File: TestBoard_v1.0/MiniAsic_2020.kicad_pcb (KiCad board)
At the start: 2 copper layers, 1 part

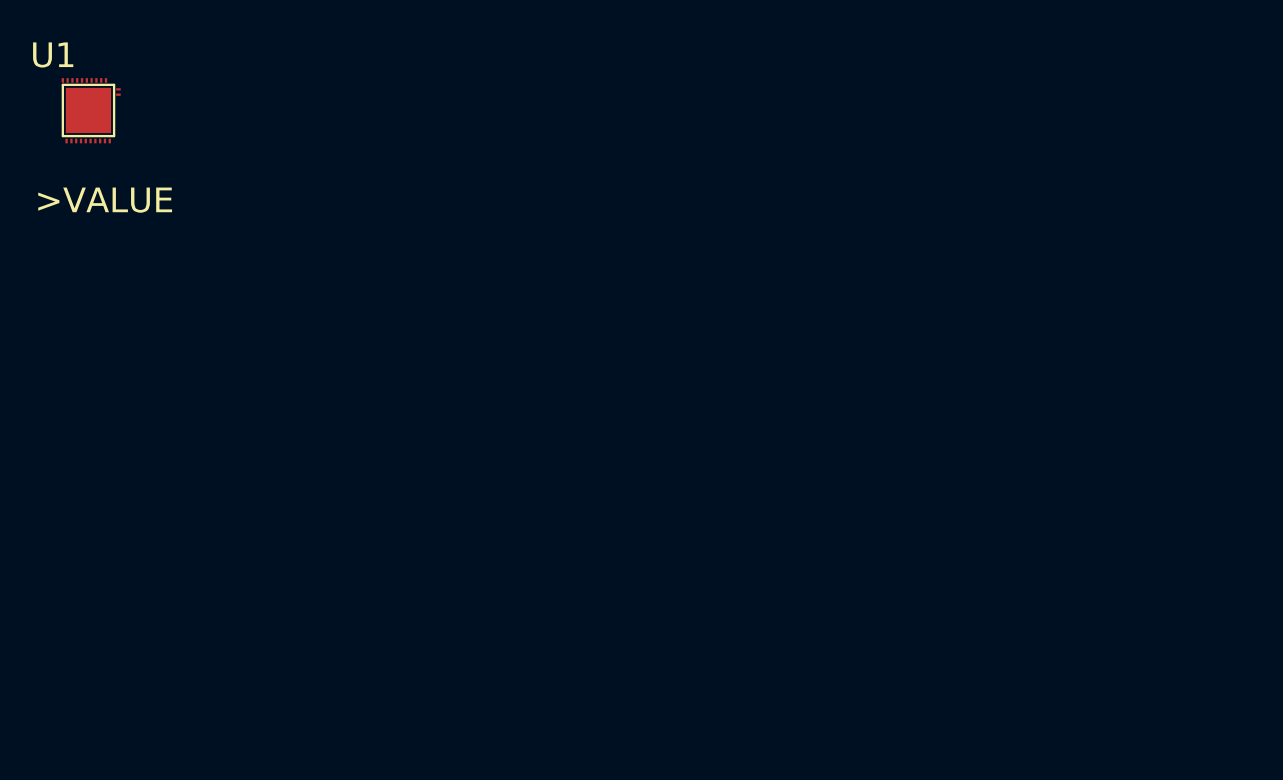
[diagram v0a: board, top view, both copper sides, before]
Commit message: Schematic update and initial placement
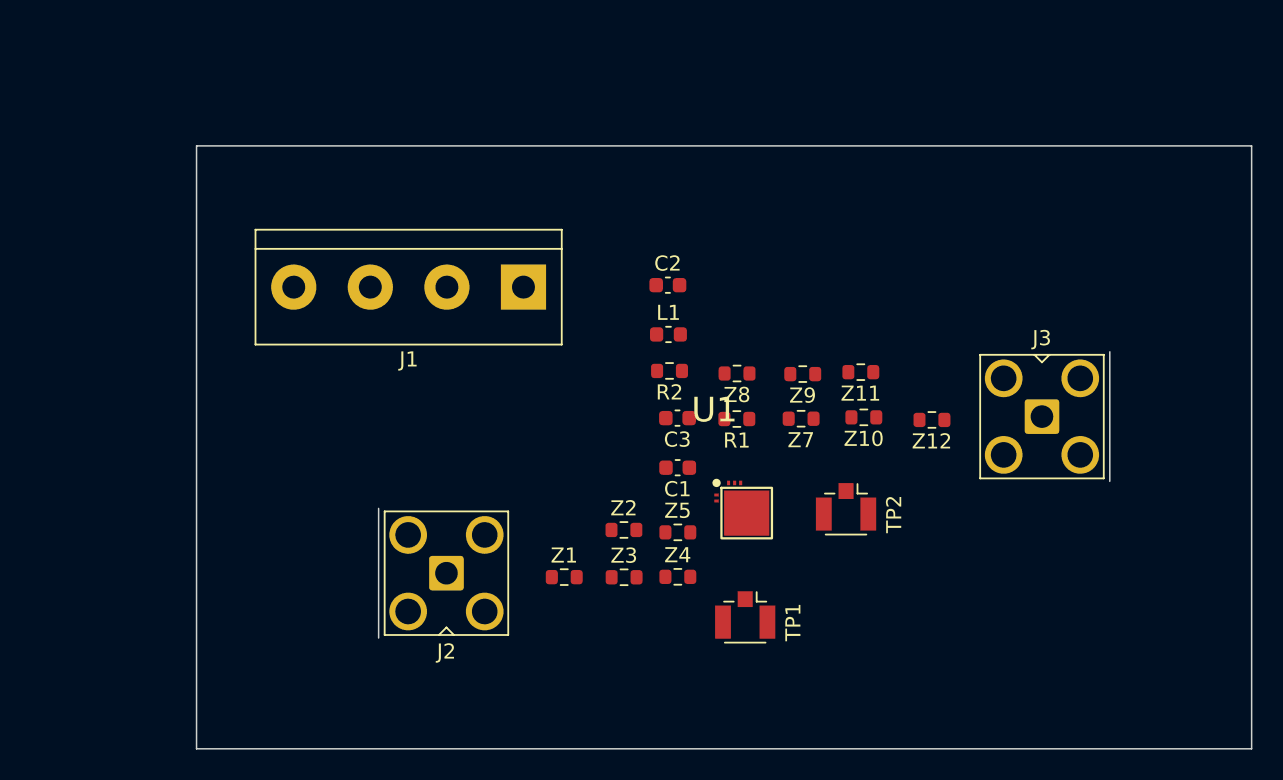
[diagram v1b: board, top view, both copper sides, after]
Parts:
- added C1: C, Capacitor_SMD:C_0603_1608Metric, F.Cu at (176.8, 121.6)
- added C2: C, Capacitor_SMD:C_0603_1608Metric, F.Cu at (176.2, 109.5)
- added C3: C, Capacitor_SMD:C_0603_1608Metric, F.Cu at (176.8, 118.3)
- added J1: Screw_Terminal_01x04, TerminalBlock:TerminalBlock_bornier-4_P5.08mm, F.Cu at (166.6, 109.6)
- added J2: Conn_Coaxial, Connector_Coaxial:SMA_Amphenol_901-143_Horizontal, F.Cu at (161.5, 128.6)
- added J3: Conn_Coaxial, Connector_Coaxial:SMA_Amphenol_901-143_Horizontal, F.Cu at (201.0, 118.2)
- added L1: L, Inductor_SMD:L_0603_1608Metric, F.Cu at (176.2, 112.8)
- added R1: R, Resistor_SMD:R_0603_1608Metric, F.Cu at (180.7, 118.4)
- added R2: R, Resistor_SMD:R_0603_1608Metric, F.Cu at (176.3, 115.2)
- added TP1: ~, Connector_Coaxial:U.FL_Hirose_U.FL-R-SMT-1_Vertical, F.Cu at (181.3, 131.4)
- added TP2: ~, Connector_Coaxial:U.FL_Hirose_U.FL-R-SMT-1_Vertical, F.Cu at (188.0, 124.2)
- added Z1: Z, Resistor_SMD:R_0603_1608Metric, F.Cu at (169.3, 128.8)
- added Z10: Z, Resistor_SMD:R_0603_1608Metric, F.Cu at (189.2, 118.2)
- added Z11: Z, Resistor_SMD:R_0603_1608Metric, F.Cu at (188.9, 115.2)
- added Z12: Z, Resistor_SMD:R_0603_1608Metric, F.Cu at (193.7, 118.4)
- added Z2: Z, Resistor_SMD:R_0603_1608Metric, F.Cu at (173.2, 125.7)
- added Z3: Z, Resistor_SMD:R_0603_1608Metric, F.Cu at (173.2, 128.9)
- added Z4: Z, Resistor_SMD:R_0603_1608Metric, F.Cu at (176.8, 128.8)
- added Z5: Z, Resistor_SMD:R_0603_1608Metric, F.Cu at (176.8, 125.9)
- added Z7: Z, Resistor_SMD:R_0603_1608Metric, F.Cu at (185.0, 118.3)
- added Z8: Z, Resistor_SMD:R_0603_1608Metric, F.Cu at (180.7, 115.3)
- added Z9: Z, Resistor_SMD:R_0603_1608Metric, F.Cu at (185.1, 115.4)
- moved U1 49.8 mm to (179.9, 123.1)
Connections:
- U1 pad 1: unconnected-(U1-IN-Pad1) -> +1V8
- U1 pad 2: GNDREF -> /IN
- U1 pad 3: +1V8 -> /VG_GATED
- U1 pad 4: /VG -> /OUT
- U1 pad 5: GNDREF -> /OUT
- U1 pad 6: /VOUT -> Net-(#PWR025-GND)
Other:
- board outline added: 70 x 40 mm

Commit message: Initial routing
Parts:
- moved TP2 18.0 mm to (205.0, 130.0), turned to 0 degrees
- moved J3 14.1 mm to (215.0, 120.0)
- moved J1 12.5 mm to (155.0, 105.0), turned to -90 degrees
- moved Z11 12.0 mm to (200.0, 120.0)
- moved Z12 11.8 mm to (205.0, 115.0)
- moved Z10 11.3 mm to (200.0, 115.0)
- moved Z9 10.9 mm to (195.0, 120.0)
- moved Z7 10.6 mm to (195.0, 115.0)
- moved Z8 10.4 mm to (190.0, 120.0)
- moved C2 10.2 mm to (180.0, 100.0)
- moved L1 8.64 mm to (180.0, 105.0)
- moved U1 7.02 mm to (186.8, 124.3)
- moved J2 6.61 mm to (155.0, 130.0)
- moved R2 6.38 mm to (180.0, 110.0)
- moved C3 4.60 mm to (180.0, 115.0)
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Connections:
- TP1 pad 1: Net-(#PWR030-GND) -> /TP1
- TP1 pad 2: /TP1 -> Net-(TP1-GND)
- TP2 pad 1: Net-(#PWR031-GND) -> /TP2
- TP2 pad 2: /TP2 -> Net-(TP2-GND)
- Z10 pad 2: Net-(Z10-Pad2) -> /TP2
- Z11 pad 1: /TP2 -> Net-(T2-Pad1)
- Z11 pad 2: Net-(Z10-Pad2) -> /TP2
- Z12 pad 2: /TP2 -> Net-(T2-Pad1)
- Z9 pad 1: Net-(Z10-Pad2) -> /TP2
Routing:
- net +1V8: track 0.00 -> 35.2 mm
- net +3.3V: track 0.00 -> 29.2 mm
- net /OUT: track 0.00 -> 28.8 mm
- net /VG: track 0.00 -> 24.3 mm
- net /TP2: track 0.00 -> 21.7 mm
- net /TP1: track 0.00 -> 17.4 mm
- net /VG_GATED: track 0.00 -> 17.2 mm
- net Net-(Z1-Pad2): track 0.00 -> 10.4 mm
- net Net-(T2-Pad1): track 0.00 -> 6.39 mm
- net /IN: track 0.00 -> 5.48 mm
- net Net-(Z8-Pad1): track 0.00 -> 3.35 mm
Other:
- board size 70 x 40 mm -> 80 x 45 mm

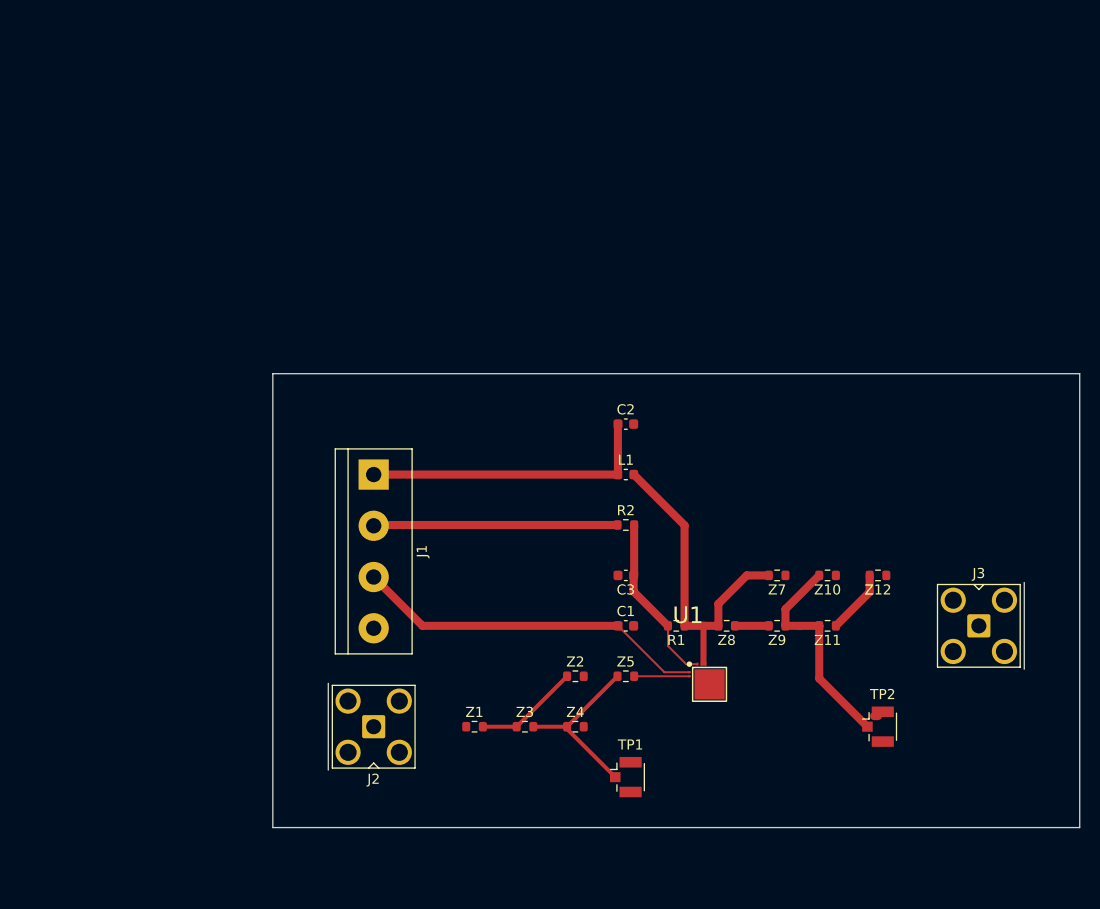
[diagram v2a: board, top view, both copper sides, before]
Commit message: New placement focused on the transmission lines
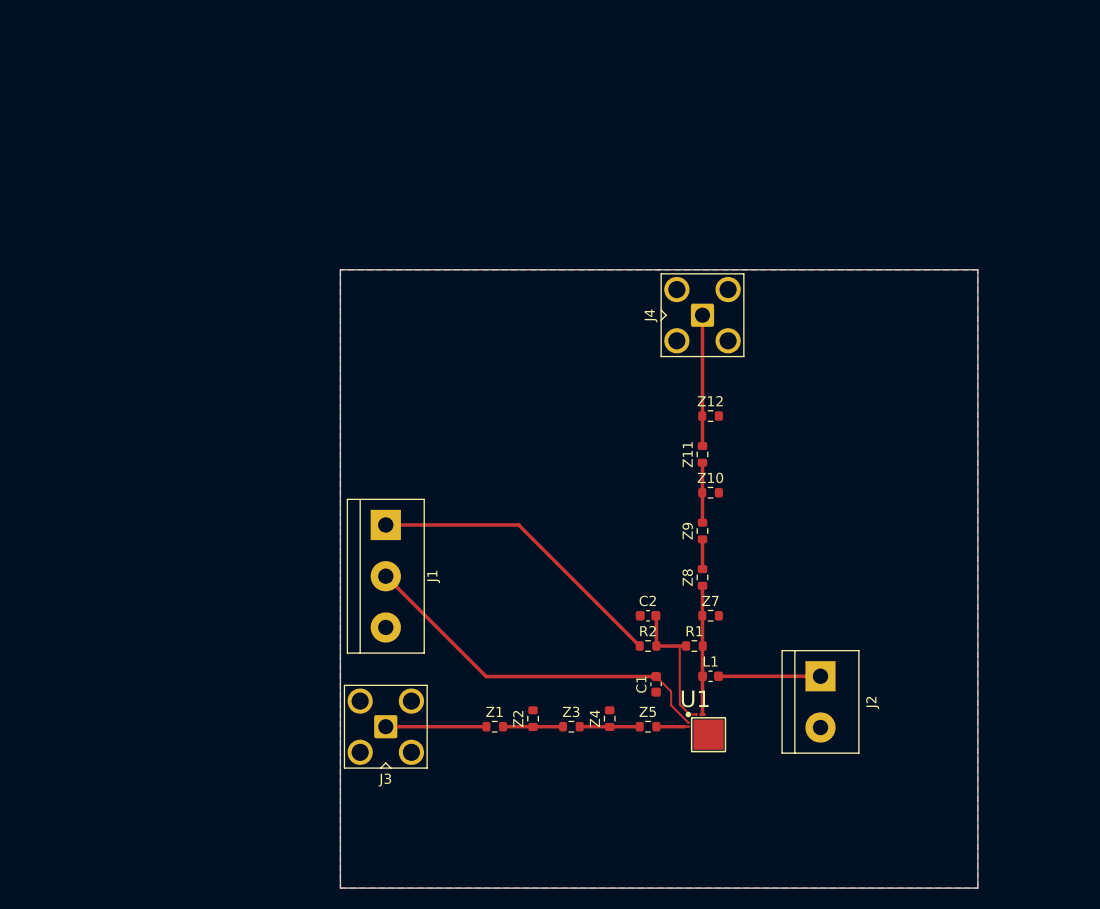
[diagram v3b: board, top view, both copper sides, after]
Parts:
- removed C3: C, Capacitor_SMD:C_0603_1608Metric
- removed TP1, TP2: ~, Connector_Coaxial:U.FL_Hirose_U.FL-R-SMT-1_Vertical
- added J4: Conn_Coaxial, Connector_Coaxial:SMA_Amphenol_901-143_Horizontal, F.Cu at (187.6, 89.2)
- J1: value Screw_Terminal_01x04 -> Screw_Terminal_01x03; footprint TerminalBlock:TerminalBlock_bornier-4_P5.08mm -> TerminalBlock:TerminalBlock_bornier-3_P5.08mm
- J2: value Conn_Coaxial -> Screw_Terminal_01x02; footprint Connector_Coaxial:SMA_Amphenol_901-143_Horizontal -> TerminalBlock:TerminalBlock_bornier-2_P5.08mm
- moved J3 59.6 mm to (156.2, 130.0), turned to 90 degrees
- moved J2 44.6 mm to (199.3, 125.0), turned to -90 degrees
- moved Z12 22.9 mm to (188.4, 99.2)
- moved L1 21.7 mm to (188.4, 125.0), turned to 180 degrees
- moved Z11 21.0 mm to (187.6, 103.0), turned to -90 degrees
- moved C2 19.1 mm to (182.2, 119.0), turned to 180 degrees
- moved Z10 14.2 mm to (188.4, 106.8)
- moved R2 12.2 mm to (182.2, 122.0)
- moved Z9 12.0 mm to (187.6, 110.6), turned to -90 degrees
- moved Z7 7.72 mm to (188.4, 119.0)
- moved C1 6.53 mm to (183.0, 125.8), turned to -90 degrees
- moved Z2 5.94 mm to (170.8, 129.2), turned to 90 degrees
- moved Z5 5.46 mm to (182.2, 130.0)
- moved Z8 5.37 mm to (187.6, 115.2), turned to -90 degrees
- moved J1 5.14 mm to (156.2, 110.0)
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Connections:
- net /TP1 renamed Net-(Z3-Pad2)
- net /TP2 renamed Net-(Z10-Pad2)
- C1 pad 2: Net-(C1-Pad2) -> GND
- C2 pad 1: +3.3V -> /VG_GATED
- C2 pad 2: Net-(C2-Pad2) -> GND
- J1 pad 1: +3.3V -> /VG
- J1 pad 2: /VG -> +1V8
- J1 pad 3: +1V8 -> GND
- J2 pad 1: Net-(J2-In) -> +3V3
- J2 pad 2: Net-(J2-Ext) -> GND
- J3 pad 2: Net-(J3-Ext) -> GND
- L1 pad 1: +3.3V -> +3V3
- U1 pad 6: Net-(U1-GND) -> unconnected-(U1-GND-Pad6)
- Z1 pad 1: Net-(T1-Pad3) -> Net-(J3-In)
- Z10 pad 1: Net-(Z10-Pad1) -> GND
- Z12 pad 1: Net-(Z12-Pad1) -> GND
- Z2 pad 2: Net-(Z2-Pad2) -> GND
- Z4 pad 2: Net-(Z4-Pad2) -> GND
- Z7 pad 1: Net-(Z7-Pad1) -> GND
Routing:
- net +3.3V: track 29.2 -> 0.00 mm
- net /OUT: track 28.8 -> 12.8 mm
- net Net-(Z10-Pad2): track 21.7 -> 5.97 mm
- net Net-(Z3-Pad2): track 17.4 -> 5.97 mm
- net +3V3: track 0.00 -> 10.1 mm
- net Net-(J3-In): track 0.00 -> 9.98 mm
- net Net-(J4-In): track 6.39 -> 13.0 mm
- net /VG: track 24.3 -> 30.1 mm
- net Net-(Z1-Pad2): track 10.4 -> 5.97 mm
- net /VG_GATED: track 17.2 -> 13.8 mm
- net /IN: track 5.48 -> 3.54 mm
- net +1V8: track 35.2 -> 36.8 mm
- added copper zone on B.Cu, net GND
- added copper zone on F.Cu, net GND
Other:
- board size 80 x 45 mm -> 63.2 x 61.3 mm

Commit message: add gnd planes and via array
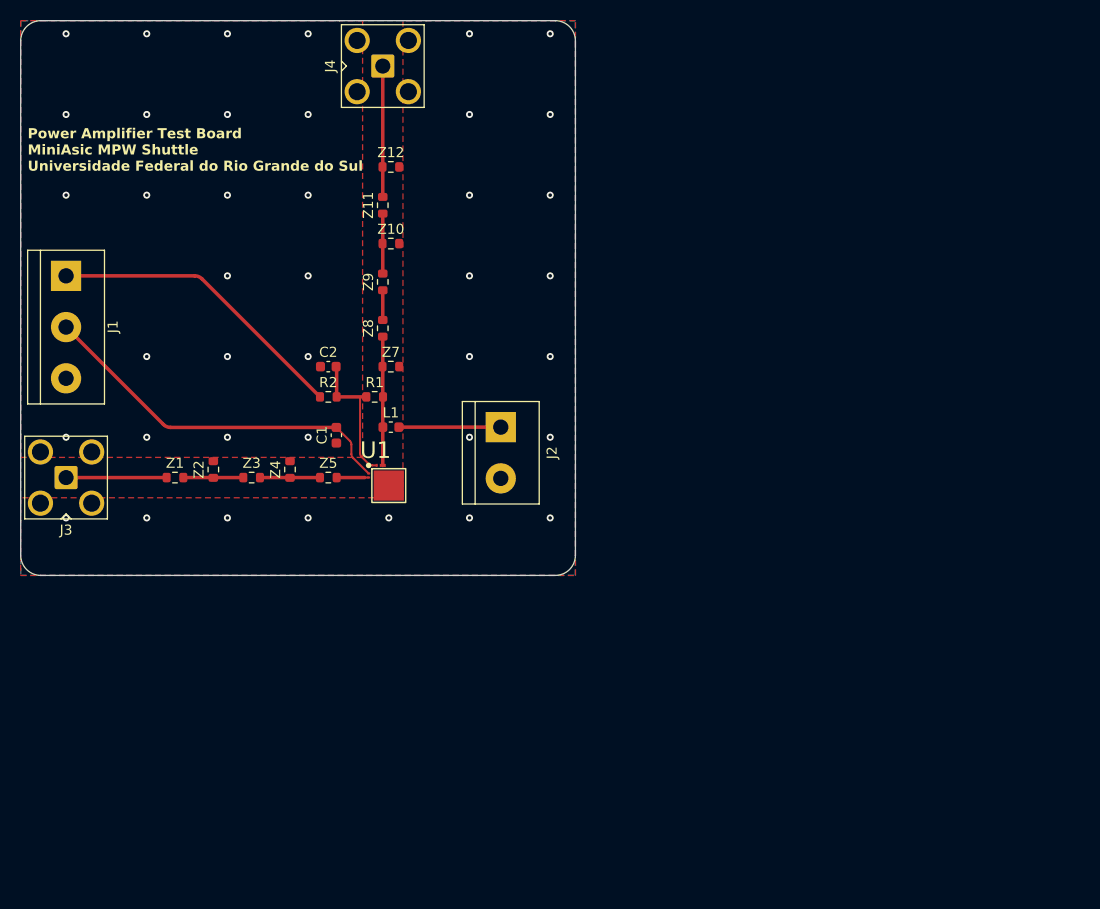
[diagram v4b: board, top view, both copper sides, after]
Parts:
- moved J2 40.2 mm to (167.6, 100.3)
- moved L1 40.2 mm to (156.7, 100.3)
- moved R1 40.2 mm to (155.1, 97.3)
- moved Z10 40.2 mm to (156.7, 82.1)
- moved Z12 40.2 mm to (156.7, 74.5)
- moved Z7 40.2 mm to (156.7, 94.3)
- moved Z2 40.2 mm to (139.1, 104.5)
- moved Z4 40.2 mm to (146.7, 104.5)
- moved C1 40.2 mm to (151.3, 101.1)
- moved C2 40.2 mm to (150.5, 94.3)
- moved J1 40.2 mm to (124.5, 85.3)
- moved J3 40.2 mm to (124.5, 105.3)
- moved J4 40.2 mm to (155.9, 64.5)
- moved R2 40.2 mm to (150.5, 97.3)
- moved Z1 40.2 mm to (135.3, 105.3)
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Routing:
- net GND: vias 0 -> 40
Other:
- board size 63.2 x 61.3 mm -> 55 x 55 mm
- board text added: "Power Amplifier Test Board MiniAsic MPW Shuttle Universidade Federal do Rio Grande do Sul"

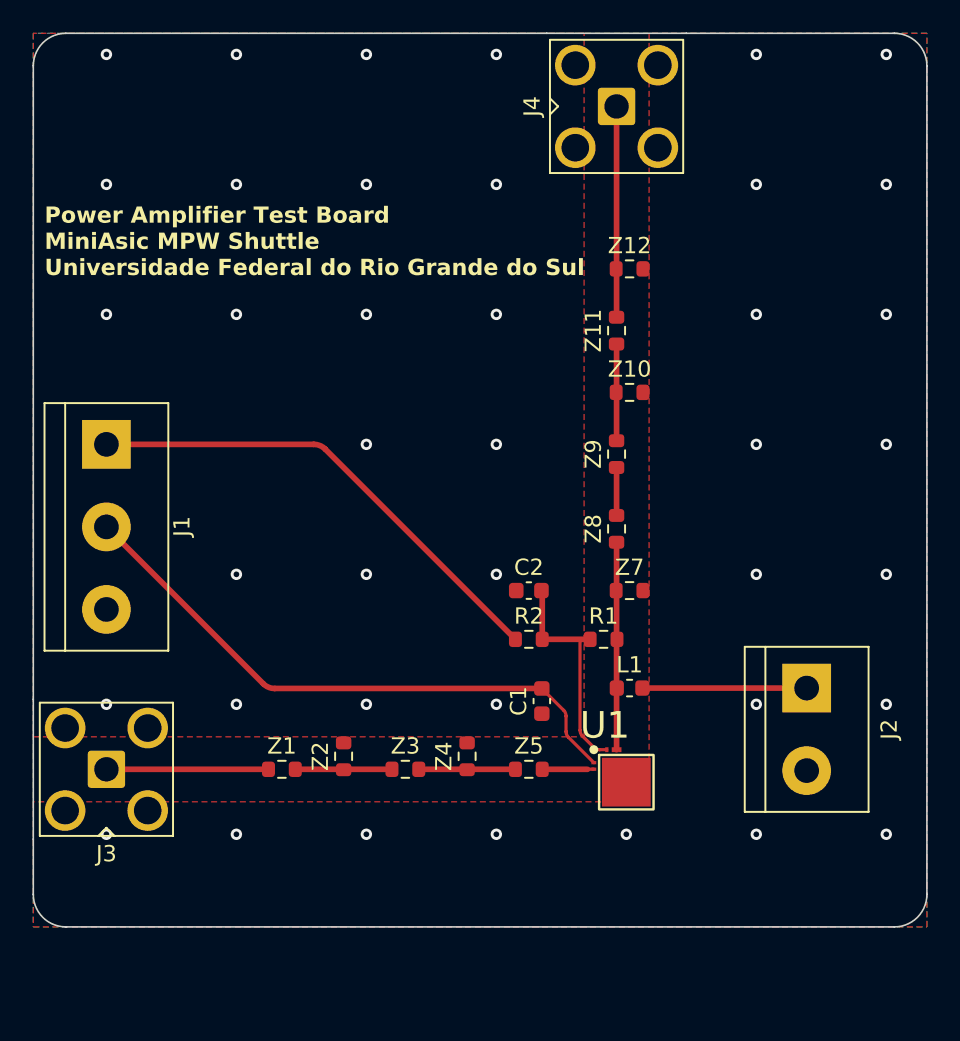
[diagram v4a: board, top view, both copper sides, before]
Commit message: Connect IC gnd pad, clean drc, add dimensions, generate gerbers, and export schematic/3d views
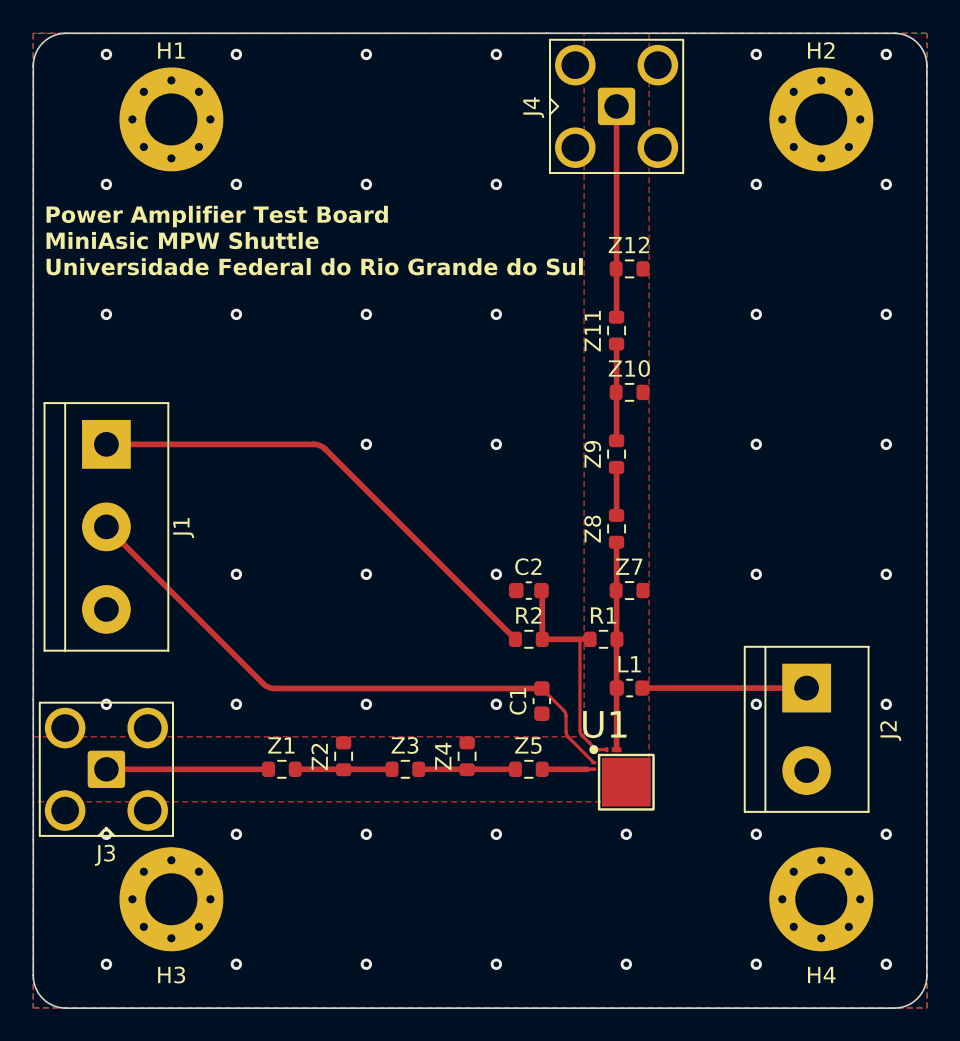
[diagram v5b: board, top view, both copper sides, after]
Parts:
- added H1: MountingHole_Pad, MountingHole:MountingHole_3.2mm_M3_Pad_Via, F.Cu at (128.5, 65.3)
- added H2: MountingHole_Pad, MountingHole:MountingHole_3.2mm_M3_Pad_Via, F.Cu at (168.5, 65.3)
- added H3: MountingHole_Pad, MountingHole:MountingHole_3.2mm_M3_Pad_Via, F.Cu at (128.5, 113.3)
- added H4: MountingHole_Pad, MountingHole:MountingHole_3.2mm_M3_Pad_Via, F.Cu at (168.5, 113.3)
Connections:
- U1 pad 6: unconnected-(U1-GND-Pad6) -> GND
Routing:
- net GND: vias 40 -> 47
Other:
- board size 55 x 55 mm -> 55 x 60 mm
